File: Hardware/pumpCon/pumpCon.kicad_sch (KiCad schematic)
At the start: 88 parts, among them J1 USB_B_Micro, J2 Conn_01x03, J3 Conn_01x02, J4 Conn_01x03, J5 Conn_01x03, J6 Conn_01x02, J7 Conn_01x02, J8 Conn_01x03, J9 Conn_01x03, U1 W25Q16JVUXIQ, U2 RP2040, U3 AP2127K-ADJ, U4 TPS92200DxRXL, U5 MCP6001R, U6 AP63357Q, Y1 12Mhz

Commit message: wip
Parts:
- L1: value 600R -> 22uH
- R1, R2: value 20R -> 10R
- R24, R25: value 1k -> 100R
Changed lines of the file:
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@@
       (effects (font (size 1.27 1.27)) (justify right))
     )
-    (property "Value" "20R" (id 1) (at 38.1 60.96 90)
+    (property "Value" "10R" (id 1) (at 38.1 60.96 90)
       (effects (font (size 1.27 1.27)) (justify right))
     )
@@
       (effects (font (size 1.27 1.27)) (justify right))
     )
-    (property "Value" "1k" (id 1) (at 234.95 140.97 90)
+    (property "Value" "100R" (id 1) (at 236.22 140.97 90)
       (effects (font (size 1.27 1.27)) (justify right))
     )
@@
       (effects (font (size 1.27 1.27)) (justify right))
     )
-    (property "Value" "20R" (id 1) (at 38.1 66.04 90)
+    (property "Value" "10R" (id 1) (at 38.1 66.04 90)
       (effects (font (size 1.27 1.27)) (justify right))
     )
@@
       (effects (font (size 1.27 1.27)) (justify right))
     )
-    (property "Value" "1k" (id 1) (at 234.95 151.13 90)
+    (property "Value" "100R" (id 1) (at 236.22 151.13 90)
       (effects (font (size 1.27 1.27)) (justify right))
     )
@@
       (effects (font (size 1.27 1.27)) (justify right))
     )
-    (property "Value" "600R" (id 1) (at 88.9 45.7199 0)
+    (property "Value" "22uH" (id 1) (at 88.9 45.7199 0)
       (effects (font (size 1.27 1.27)) (justify right))
     )
@@
     )
     (path "/b61ec1ed-0168-4f25-9f19-921cc4714e44"
-      (reference "L1") (unit 1) (value "600R") (footprint "Inductor_SMD:L_0603_1608Metric")
+      (reference "L1") (unit 1) (value "22uH") (footprint "Inductor_SMD:L_0603_1608Metric")
     )
     (path "/71e2a85c-5bc4-4103-8314-a44234d2543f"
@@
     )
     (path "/63900c90-3411-4f47-a561-1b9315c23a54"
-      (reference "R1") (unit 1) (value "20R") (footprint "Resistor_SMD:R_0603_1608Metric")
+      (reference "R1") (unit 1) (value "10R") (footprint "Resistor_SMD:R_0603_1608Metric")
     )
     (path "/87e568d4-5cea-49a3-bb17-5754ec4c853c"
-      (reference "R2") (unit 1) (value "20R") (footprint "Resistor_SMD:R_0603_1608Metric")
+      (reference "R2") (unit 1) (value "10R") (footprint "Resistor_SMD:R_0603_1608Metric")
     )
     (path "/9f1ffac8-47b9-4555-9727-f60425405e62"
@@
     )
     (path "/64e4c45e-2790-461b-8350-3a4b913f4f00"
-      (reference "R24") (unit 1) (value "1k") (footprint "Resistor_SMD:R_0603_1608Metric")
+      (reference "R24") (unit 1) (value "100R") (footprint "Resistor_SMD:R_0603_1608Metric")
     )
     (path "/ab4bff62-ea6d-41b4-b863-5a9115e520d1"
-      (reference "R25") (unit 1) (value "1k") (footprint "Resistor_SMD:R_0603_1608Metric")
+      (reference "R25") (unit 1) (value "100R") (footprint "Resistor_SMD:R_0603_1608Metric")
     )
     (path "/ef3fe419-54ef-4cc2-a084-79bf7e3147f8"

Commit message: wip
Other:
- note added: "Notiz für V2.0: -) Spannunsgmessung 24V sinvvol -) Richtige Stepper driver"
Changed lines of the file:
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@@
     (stroke (width 0) (type default) (color 0 0 0 0))
+  )
+  (text "Notiz für V2.0:\n-) Spannunsgmessung 24V sinvvol\n-) Richtige Stepper driver"
+    (at 106.68 149.86 0)
+    (effects (font (size 1.27 1.27)) (justify left bottom))
   )
   (text "PWM3A\nPWM3B" (at 87.63 121.92 0)

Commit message: wip
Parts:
- R14, R8: value 100k -> 62k
- R15, R9: value 62k -> 100k
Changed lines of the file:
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@@
       (effects (font (size 1.27 1.27)) (justify right))
     )
-    (property "Value" "100k" (id 1) (at 148.59 171.45 90)
+    (property "Value" "62k" (id 1) (at 148.59 172.72 90)
       (effects (font (size 1.27 1.27)) (justify right))
     )
@@
       (effects (font (size 1.27 1.27)) (justify right))
     )
-    (property "Value" "100k" (id 1) (at 102.87 171.45 90)
+    (property "Value" "62k" (id 1) (at 102.87 172.72 90)
       (effects (font (size 1.27 1.27)) (justify right))
     )
@@
       (effects (font (size 1.27 1.27)) (justify right))
     )
-    (property "Value" "62k" (id 1) (at 148.59 180.34 90)
+    (property "Value" "100k" (id 1) (at 148.59 179.07 90)
       (effects (font (size 1.27 1.27)) (justify right))
     )
@@
       (effects (font (size 1.27 1.27)) (justify right))
     )
-    (property "Value" "62k" (id 1) (at 102.87 180.34 90)
+    (property "Value" "100k" (id 1) (at 102.87 179.07 90)
       (effects (font (size 1.27 1.27)) (justify right))
     )
@@
       (reference "#PWR0226") (unit 1) (value "+3V3") (footprint "")
     )
-    (path "/6d98db2c-24de-4eeb-98a9-cd90e5c5e5a6/4c2f1929-422b-4330-85e5-c7b2f9456afc"
-      (reference "#PWR0227") (unit 1) (value "GND") (footprint "")
-    )
-    (path "/6d98db2c-24de-4eeb-98a9-cd90e5c5e5a6/efb163f3-06d2-4762-9e83-c005aa6f3223"
-      (reference "#PWR0228") (unit 1) (value "GND") (footprint "")
-    )
     (path "/6d98db2c-24de-4eeb-98a9-cd90e5c5e5a6/743495f3-5493-4911-b703-ec409f8a7119"
       (reference "#PWR0229") (unit 1) (value "GND") (footprint "")
     )
-    (path "/6d98db2c-24de-4eeb-98a9-cd90e5c5e5a6/80230112-870d-4263-80d8-ed5fa27f01b0"
-      (reference "#PWR0230") (unit 1) (value "GND") (footprint "")
-    )
-    (path "/6d98db2c-24de-4eeb-98a9-cd90e5c5e5a6/1dfbfad9-95b1-42c9-b51d-ae7562a260cf"
-      (reference "#PWR0231") (unit 1) (value "GND") (footprint "")
-    )
     (path "/6d98db2c-24de-4eeb-98a9-cd90e5c5e5a6/6e2fc237-b99b-4174-ae4b-1c3272be2c70"
       (reference "#PWR0232") (unit 1) (value "+24V") (footprint "")
@@
     )
     (path "/6d98db2c-24de-4eeb-98a9-cd90e5c5e5a6/c3d2f714-beb4-4f1c-b41a-98b8c767b35f"
-      (reference "L6") (unit 1) (value "33µ") (footprint "Inductor_SMD:L_12x12mm_H8mm")
+      (reference "L6") (unit 1) (value "100u") (footprint "Inductor_SMD:L_12x12mm_H8mm")
     )
     (path "/6d98db2c-24de-4eeb-98a9-cd90e5c5e5a6/b6ad762f-3827-4deb-ae04-2e93887c0d4a"
-      (reference "L7") (unit 1) (value "33µ") (footprint "Inductor_SMD:L_12x12mm_H8mm")
+      (reference "L7") (unit 1) (value "100u") (footprint "Inductor_SMD:L_12x12mm_H8mm")
     )
     (path "/63900c90-3411-4f47-a561-1b9315c23a54"
@@
     )
     (path "/2b4f270f-803d-4120-abf1-dafa5b16c19d"
-      (reference "R8") (unit 1) (value "100k") (footprint "Resistor_SMD:R_0603_1608Metric")
+      (reference "R8") (unit 1) (value "62k") (footprint "Resistor_SMD:R_0603_1608Metric")
     )
     (path "/9d2d6d68-8ce6-42e9-b34a-650d02a73d9e"
-      (reference "R9") (unit 1) (value "62k") (footprint "Resistor_SMD:R_0603_1608Metric")
+      (reference "R9") (unit 1) (value "100k") (footprint "Resistor_SMD:R_0603_1608Metric")
     )
     (path "/b818538a-853d-4f8e-bb9d-c5b9db19b61b"
@@
     )
     (path "/1fdd1952-f51f-44e9-9713-583f0576d001"
-      (reference "R14") (unit 1) (value "100k") (footprint "Resistor_SMD:R_0603_1608Metric")
+      (reference "R14") (unit 1) (value "62k") (footprint "Resistor_SMD:R_0603_1608Metric")
     )
     (path "/4b9c6311-7c2f-4843-b3eb-dec7d4058033"
-      (reference "R15") (unit 1) (value "62k") (footprint "Resistor_SMD:R_0603_1608Metric")
+      (reference "R15") (unit 1) (value "100k") (footprint "Resistor_SMD:R_0603_1608Metric")
     )
     (path "/4580eefb-df2d-4a58-85d5-0d2cf57c26fb"

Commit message: pumpCon fully work now
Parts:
- added C? (x3): 1nF, Capacitor_SMD:C_0603_1608Metric, symbol Device:C
- added R? (x3): 10k, Resistor_SMD:R_0603_1608Metric, symbol Device:R
- added R?: 1k, Resistor_SMD:R_0603_1608Metric, symbol Device:R
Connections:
- net +24V: now also R?.2
- net GND: now also C?.2, C?.2, C?.2, R?.1
- net pumpDrivers/Isens0: now also R?.2; no longer U2.38 (GPIO26_ADC0)
- net pumpDrivers/Isens1: now also R?.2; no longer U2.39 (GPIO27_ADC1)
- net 24V_sens: now reaches U2.40 (GPIO28_ADC2)
- net 24V_sens: now also C?.1, R?.1, R?.2
- new net: C?.1, R?.1, U2.38 (GPIO26_ADC0)
- new net: C?.1, R?.1, U2.39 (GPIO27_ADC1)
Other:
- moved on the sheet: R11, R12

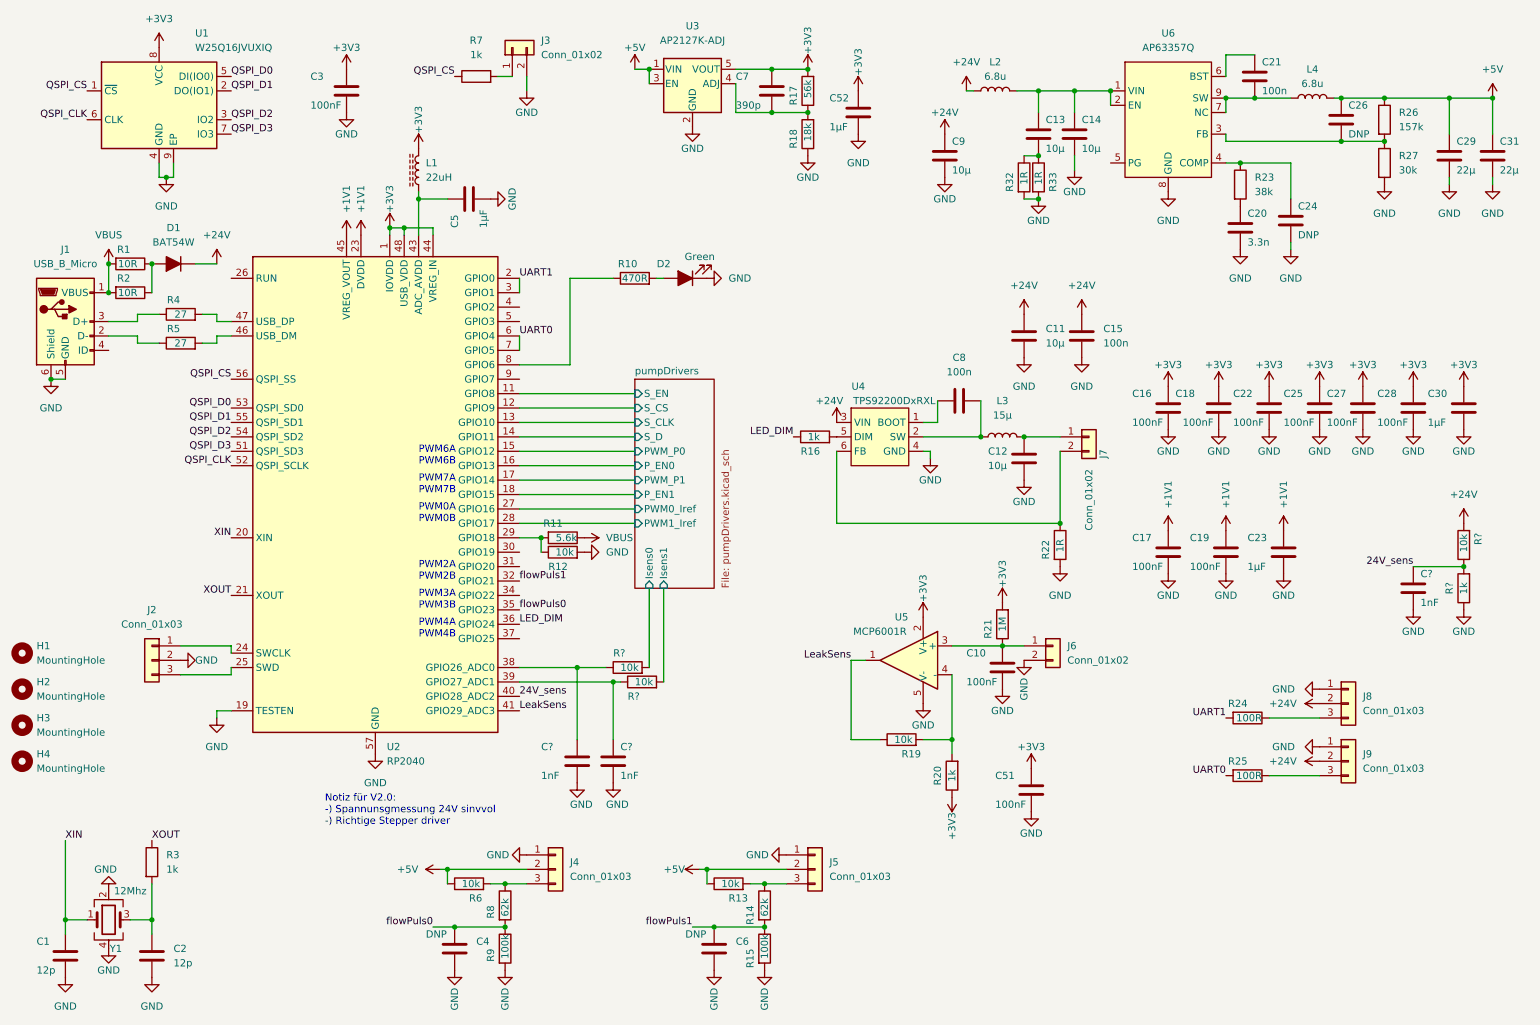
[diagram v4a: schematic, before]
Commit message: modified motor output
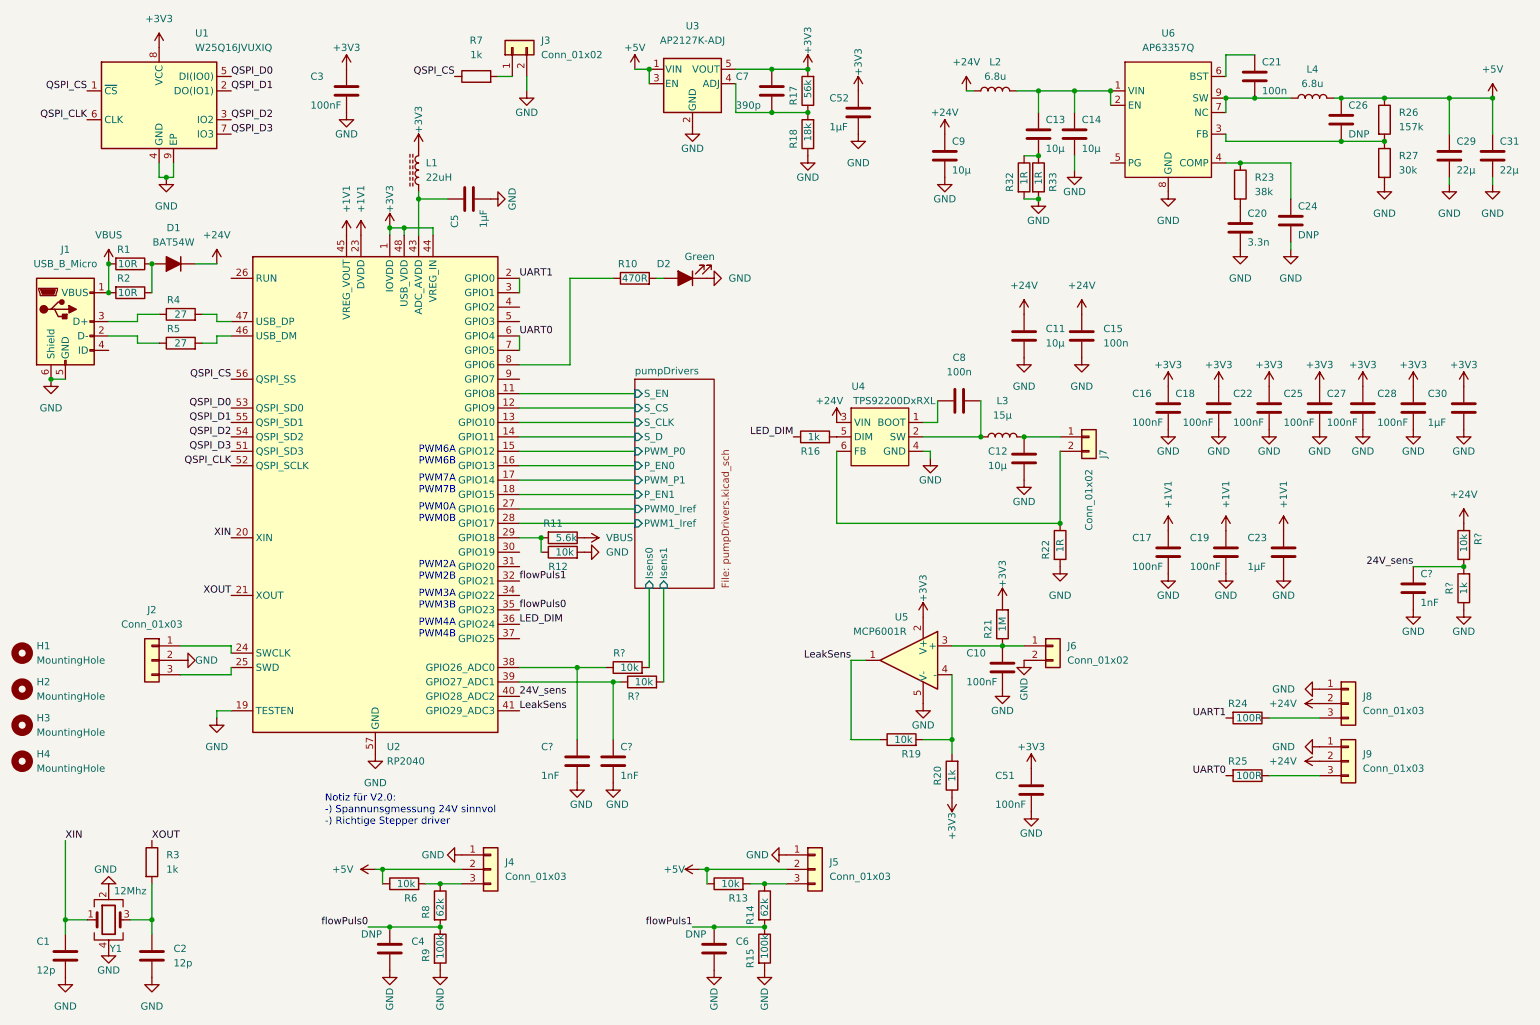
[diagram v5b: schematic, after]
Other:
- note added: "Notiz für V2.0: -) Spannunsgmessung 24V sinnvol -) Richtige Stepper driver"
- note removed: "Notiz für V2.0: -) Spannunsgmessung 24V sinvvol -) Richtige Stepper driver"
- moved on the sheet: C4, J4, R6, R8, R9
